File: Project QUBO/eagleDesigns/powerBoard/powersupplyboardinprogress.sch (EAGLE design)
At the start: 11 parts

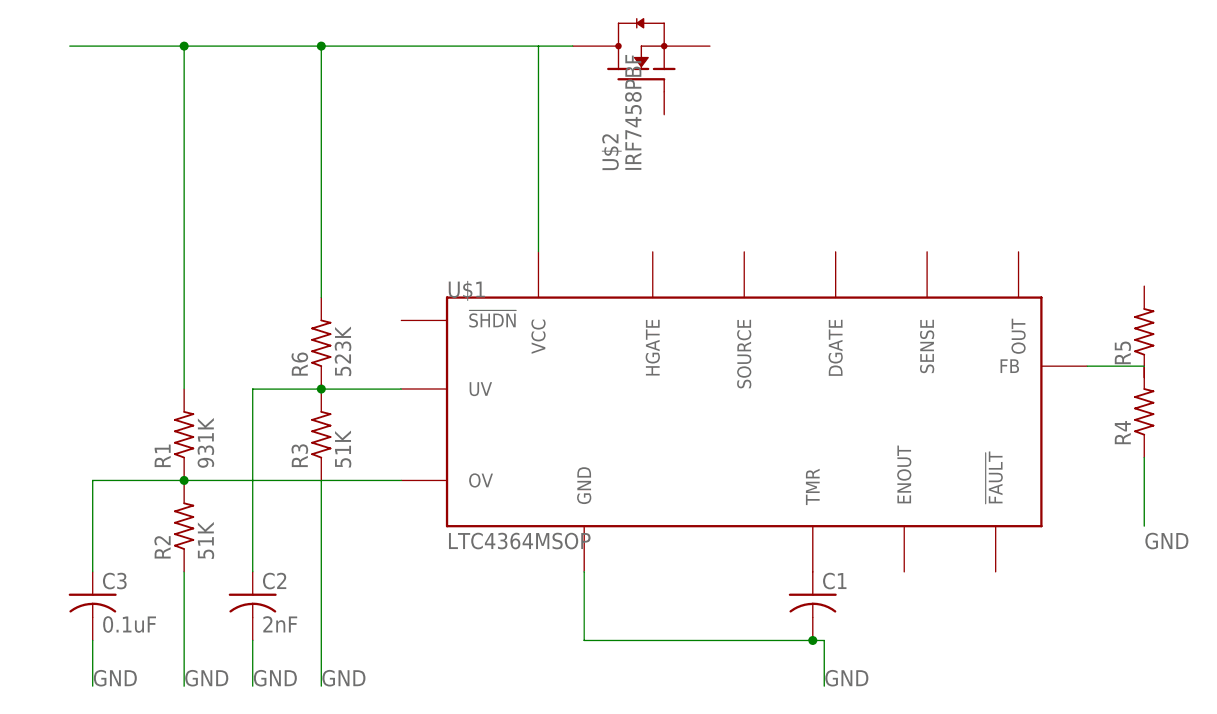
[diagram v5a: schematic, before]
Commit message: 
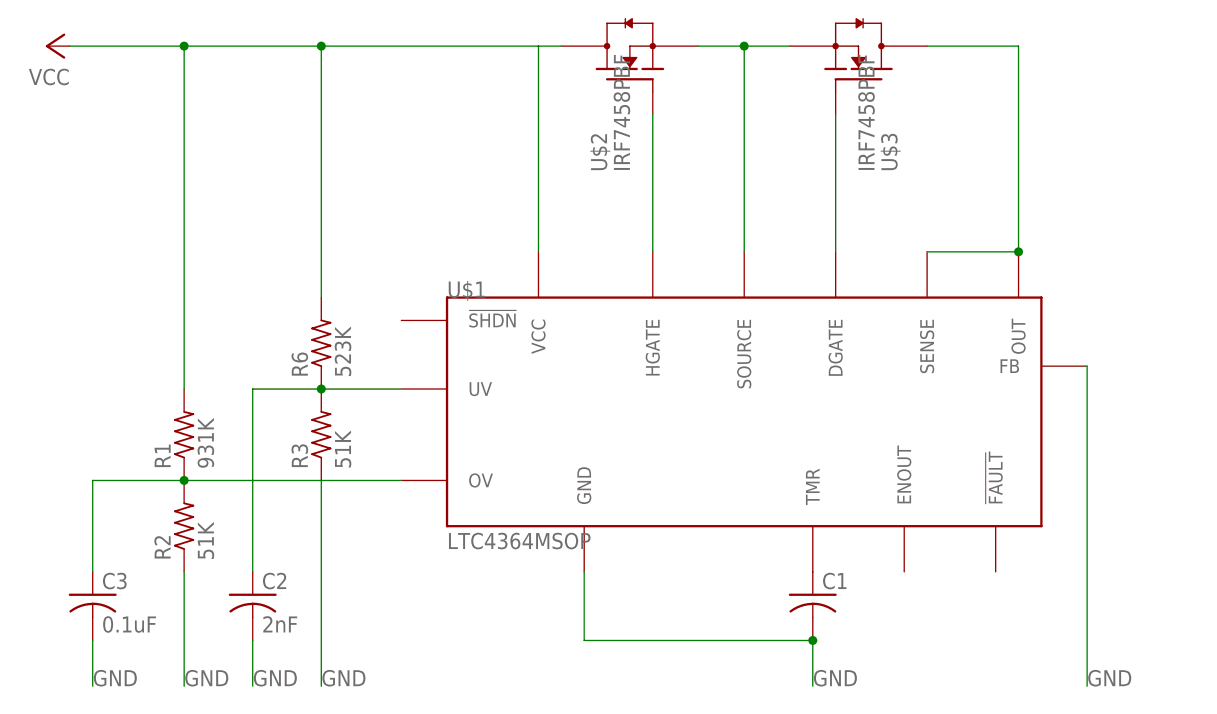
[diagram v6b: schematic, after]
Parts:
- removed R4, R5: (no value), resistor:R-US_R0805
- added U$3: IRF7458PBF, transistor-fet:IRF7458PBF
- U$2: SPICEPREFIX (none) -> M
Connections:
- net N$7 renamed VCC
- removed net N$4: R4.2, U$1.FB
- new net N$1: U$1.DGATE, U$3.G
- new net N$10: U$1.HGATE, U$2.G
- new net N$2: U$1.SOURCE, U$2.S, U$3.S
- new net N$9: U$1.OUT, U$1.SENSE, U$3.D
- net GND: now also U$1.FB; no longer R4.1
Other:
- moved on the sheet: U$2
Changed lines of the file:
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@@
 <?xml version="1.0" encoding="utf-8"?>
 <!DOCTYPE eagle SYSTEM "eagle.dtd">
-<eagle version="8.4.1">
+<eagle version="8.4.2">
 <drawing>
 <settings>
@@
 <setting verticaltext="up"/>
 </settings>
-<grid distance="0.1" unitdist="inch" unit="inch" style="lines" multiple="1" display="no" altdistance="0.01" altunitdist="inch" altunit="inch"/>
+<grid distance="0.05" unitdist="inch" unit="inch" style="lines" multiple="1" display="no" altdistance="0.01" altunitdist="inch" altunit="inch"/>
 <layers>
 <layer number="1" name="Top" color="4" fill="1" visible="no" active="no"/>
@@
 <part name="U$1" library="linear" deviceset="LTC4364" device="MSOP"/>
 <part name="C1" library="resistor" deviceset="C-US" device="C0805"/>
-<part name="R4" library="resistor" deviceset="R-US_" device="R0805"/>
-<part name="R5" library="resistor" deviceset="R-US_" device="R0805"/>
 <part name="R1" library="resistor" deviceset="R-US_" device="M0805" value="931K"/>
 <part name="R2" library="resistor" deviceset="R-US_" device="M0805" value="51K"/>
@@
 <attribute name="SPICEPREFIX" value="C"/>
 </part>
-<part name="U$2" library="transistor-fet" deviceset="IRF7458PBF" device=""/>
+<part name="U$2" library="transistor-fet" deviceset="IRF7458PBF" device="">
+<attribute name="SPICEPREFIX" value="M"/>
+</part>
+<part name="U$3" library="transistor-fet" deviceset="IRF7458PBF" device=""/>
+<part name="BAT1" library="supply1" deviceset="VCC" device=""/>
 </parts>
 <sheets>
@@
 <instance part="U$1" gate="G$1" x="74.93" y="76.2"/>
 <instance part="C1" gate="G$1" x="82.55" y="55.88"/>
-<instance part="R4" gate="G$1" x="119.38" y="76.2" rot="R90"/>
-<instance part="R5" gate="G$1" x="119.38" y="85.09" rot="R90"/>
 <instance part="R1" gate="G$1" x="12.7" y="73.66" rot="R90"/>
 <instance part="R2" gate="G$1" x="12.7" y="63.5" rot="R90"/>
@@
 <instance part="C2" gate="G$1" x="20.32" y="55.88"/>
 <instance part="C3" gate="G$1" x="2.54" y="55.88"/>
-<instance part="U$2" gate="G$1" x="63.5" y="114.3" rot="R90"/>
+<instance part="U$2" gate="G$1" x="62.23" y="114.3" rot="R90"/>
+<instance part="U$3" gate="G$1" x="87.63" y="114.3" rot="MR90"/>
+<instance part="BAT1" gate="VCC" x="-2.54" y="116.84" rot="R90"/>
 </instances>
 <busses>
@@
 <net name="GND" class="0">
 <segment>
-<pinref part="R4" gate="G$1" pin="1"/>
-<wire x1="119.38" y1="71.12" x2="119.38" y2="63.5" width="0.1524" layer="91"/>
-<label x="119.38" y="60.96" size="1.778" layer="95"/>
-</segment>
-<segment>
 <pinref part="C1" gate="G$1" pin="2"/>
 <pinref part="U$1" gate="G$1" pin="GND"/>
 <wire x1="82.55" y1="50.8" x2="57.15" y2="50.8" width="0.1524" layer="91"/>
 <wire x1="57.15" y1="50.8" x2="57.15" y2="58.42" width="0.1524" layer="91"/>
-<wire x1="82.55" y1="50.8" x2="83.82" y2="50.8" width="0.1524" layer="91"/>
-<wire x1="83.82" y1="50.8" x2="83.82" y2="45.72" width="0.1524" layer="91"/>
+<wire x1="82.55" y1="50.8" x2="82.55" y2="45.72" width="0.1524" layer="91"/>
 <junction x="82.55" y="50.8"/>
-<label x="83.82" y="45.72" size="1.778" layer="95"/>
+<label x="82.55" y="45.72" size="1.778" layer="95"/>
 </segment>
 <segment>
@@
 <label x="2.54" y="45.72" size="1.778" layer="95"/>
 </segment>
+<segment>
+<pinref part="U$1" gate="G$1" pin="FB"/>
+<wire x1="113.03" y1="81.28" x2="113.03" y2="45.72" width="0.1524" layer="91"/>
+<label x="113.03" y="45.72" size="1.778" layer="95"/>
+</segment>
 </net>
 <net name="N$3" class="0">
@@
 <pinref part="U$1" gate="G$1" pin="TMR"/>
 <pinref part="C1" gate="G$1" pin="1"/>
-</segment>
-</net>
-<net name="N$4" class="0">
-<segment>
-<pinref part="U$1" gate="G$1" pin="FB"/>
-<wire x1="113.03" y1="81.28" x2="119.38" y2="81.28" width="0.1524" layer="91"/>
-<pinref part="R4" gate="G$1" pin="2"/>
 </segment>
 </net>
@@
 </segment>
 </net>
-<net name="N$7" class="0">
+<net name="N$1" class="0">
+<segment>
+<pinref part="U$1" gate="G$1" pin="DGATE"/>
+<pinref part="U$3" gate="G$1" pin="G"/>
+<wire x1="85.09" y1="93.98" x2="85.09" y2="109.22" width="0.1524" layer="91"/>
+</segment>
+</net>
+<net name="N$2" class="0">
+<segment>
+<pinref part="U$2" gate="G$1" pin="S"/>
+<pinref part="U$3" gate="G$1" pin="S"/>
+<wire x1="69.85" y1="116.84" x2="74.93" y2="116.84" width="0.1524" layer="91"/>
+<pinref part="U$1" gate="G$1" pin="SOURCE"/>
+<wire x1="74.93" y1="116.84" x2="80.01" y2="116.84" width="0.1524" layer="91"/>
+<wire x1="74.93" y1="93.98" x2="74.93" y2="116.84" width="0.1524" layer="91"/>
+<junction x="74.93" y="116.84"/>
+</segment>
+</net>
+<net name="N$9" class="0">
+<segment>
+<pinref part="U$3" gate="G$1" pin="D"/>
+<wire x1="95.25" y1="116.84" x2="105.41" y2="116.84" width="0.1524" layer="91"/>
+<pinref part="U$1" gate="G$1" pin="SENSE"/>
+<pinref part="U$1" gate="G$1" pin="OUT"/>
+<wire x1="95.25" y1="93.98" x2="105.41" y2="93.98" width="0.1524" layer="91"/>
+<wire x1="105.41" y1="93.98" x2="105.41" y2="116.84" width="0.1524" layer="91"/>
+<junction x="105.41" y="93.98"/>
+</segment>
+</net>
+<net name="N$10" class="0">
+<segment>
+<pinref part="U$1" gate="G$1" pin="HGATE"/>
+<pinref part="U$2" gate="G$1" pin="G"/>
+<wire x1="64.77" y1="93.98" x2="64.77" y2="109.22" width="0.1524" layer="91"/>
+</segment>
+</net>
+<net name="VCC" class="0">
 <segment>
 <pinref part="R6" gate="G$1" pin="2"/>
@@
 <wire x1="12.7" y1="116.84" x2="0" y2="116.84" width="0.1524" layer="91"/>
 <junction x="12.7" y="116.84"/>
-<wire x1="55.88" y1="116.84" x2="52.07" y2="116.84" width="0.1524" layer="91"/>
+<wire x1="54.61" y1="116.84" x2="52.07" y2="116.84" width="0.1524" layer="91"/>
 <pinref part="U$2" gate="G$1" pin="D"/>
-</segment>
-</net>
+<pinref part="BAT1" gate="VCC" pin="VCC"/>
+</segment>
+</net>

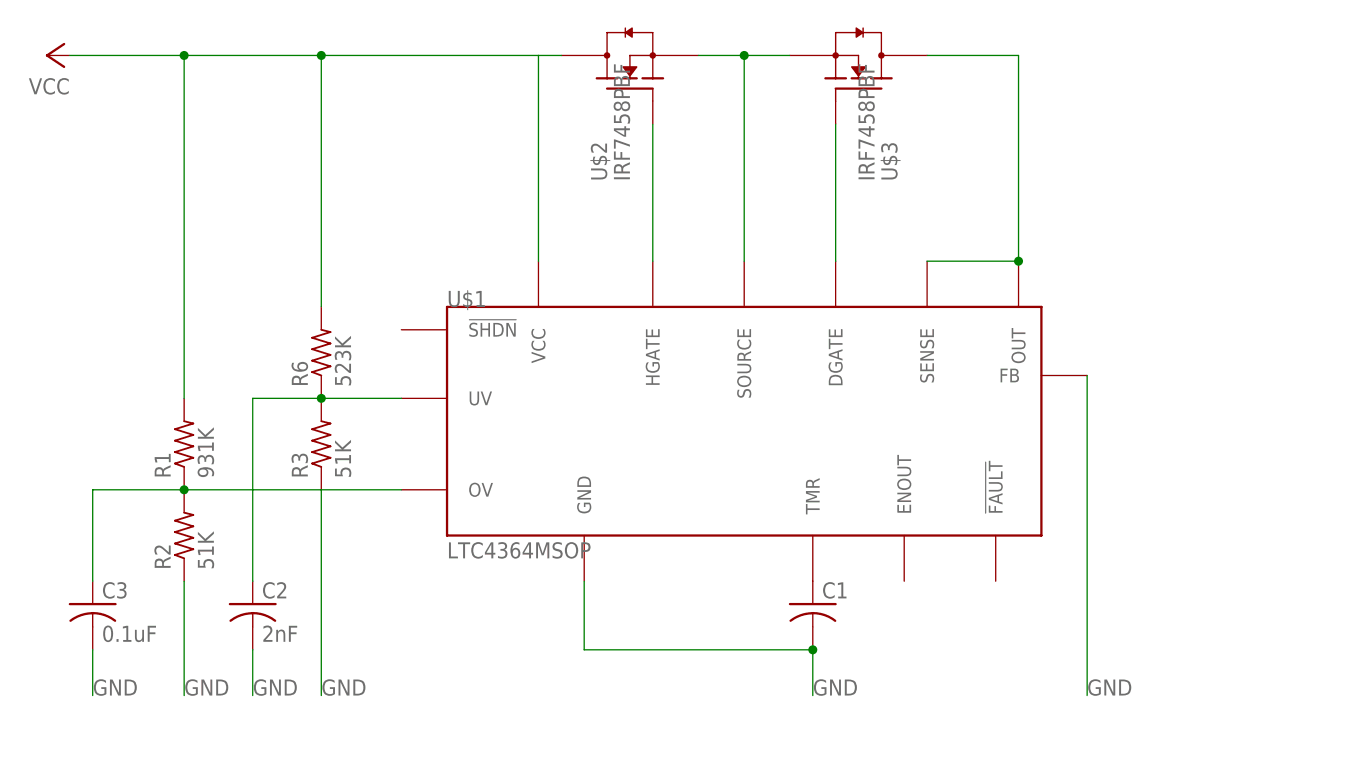
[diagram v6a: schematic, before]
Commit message: Redesigned the battery balancing board
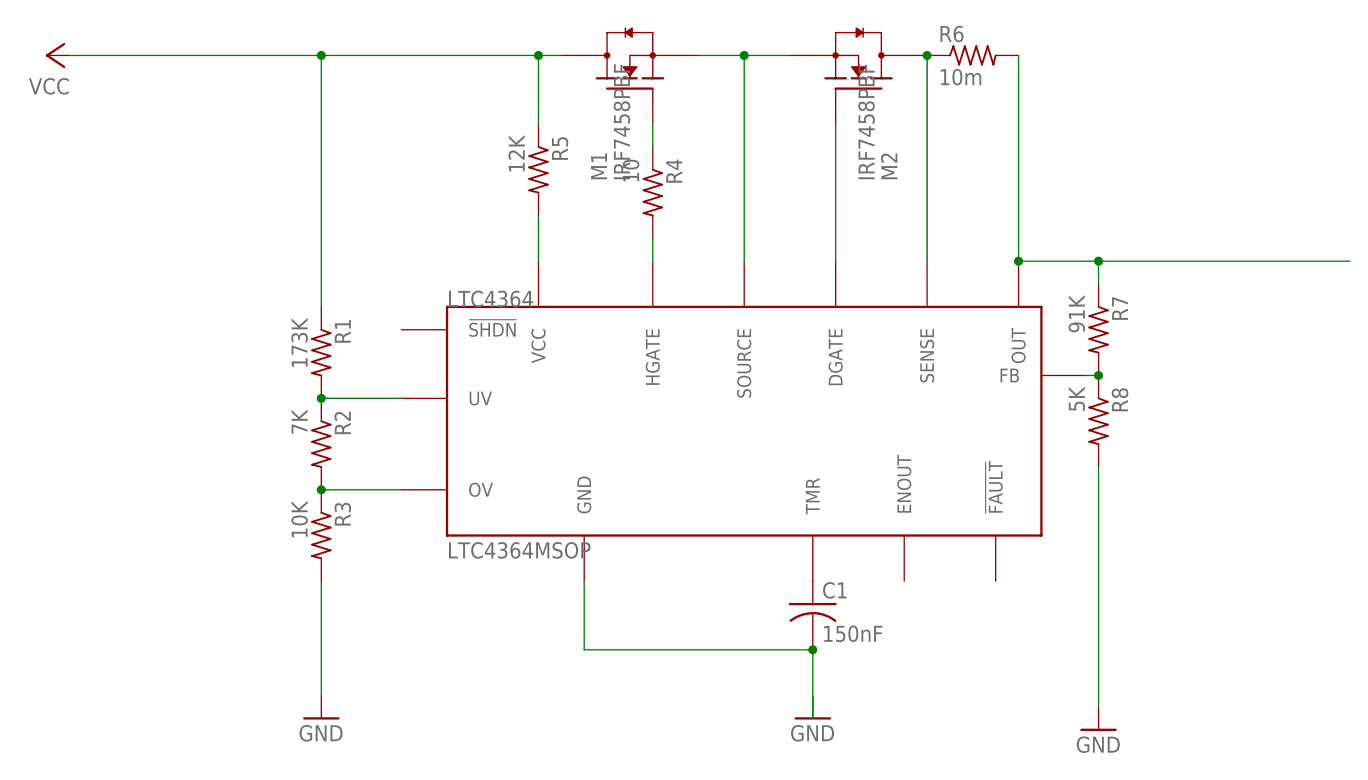
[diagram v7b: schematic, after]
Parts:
- removed C2: 2nF, resistor:C-USC0805
- removed C3: 0.1uF, resistor:C-USC0805
- added R4: 10, resistor:R-US_R0805
- added R5: 12K, resistor:R-US_R0805
- added R7: 91K, resistor:R-US_R0805
- added R8: 5K, resistor:R-US_R0805
- C1: value (none) -> 150nF; SPICEPREFIX (none) -> C
- LTC4364: SPICEPREFIX (none) -> X
- M2: SPICEPREFIX (none) -> M
- R1: value 931K -> 173K; device resistor:R-US_M0805 -> resistor:R-US_R0805
- R2: value 51K -> 7K; device resistor:R-US_M0805 -> resistor:R-US_R0805
- R3: value 51K -> 10K; device resistor:R-US_M0805 -> resistor:R-US_R0805
- R6: value 523K -> 10m; device resistor:R-US_M0805 -> resistor:R-US_R0805
- renumbered U$1 to LTC4364, U$2 to M1, U$3 to M2
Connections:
- new net N$11: LTC4364.SENSE, M2.D, R6.1
- new net N$4: LTC4364.UV, R1.2, R2.1
- new net N$7: LTC4364.FB, R7.2, R8.1
- new net N$8: LTC4364.HGATE, R4.2
- net GND: now also R3.2, R8.2; no longer C2.2, C3.2, LTC4364.FB, R2.1, R3.1
- net N$10: now also LTC4364.VCC, R5.2; no longer LTC4364.HGATE, M1.G
- net N$5: now also LTC4364.OV, R2.2, R3.1; no longer C2.1, LTC4364.UV, R3.2, R6.1
- net N$6: now also M1.G, R4.1; no longer C3.1, LTC4364.OV, R1.1, R2.2
- net N$9: now also R6.2, R7.1; no longer LTC4364.SENSE, M2.D
- net VCC: now also R1.1, R5.1; no longer LTC4364.VCC, R1.2, R6.2
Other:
- moved on the sheet: R1, R2, R3, R6
